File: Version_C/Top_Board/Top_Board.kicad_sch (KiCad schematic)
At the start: 12 parts, among them J1 90_Deg_Conn, J2 ADS1015, J4 90_Deg_Conn, U1 T-Display-S3

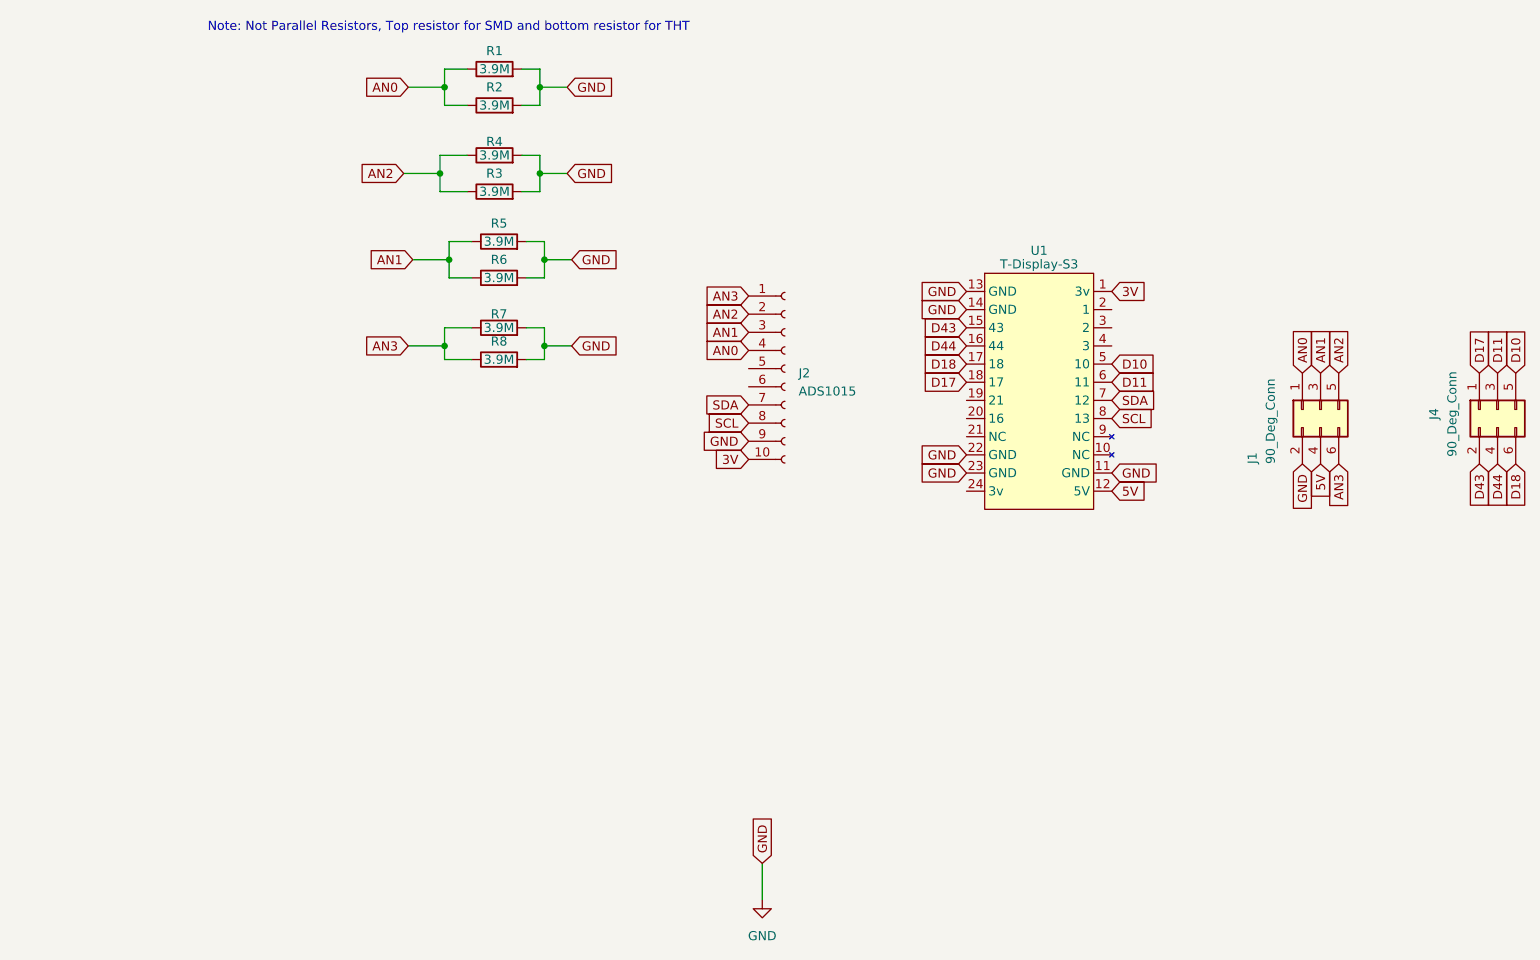
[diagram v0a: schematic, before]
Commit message: fixed directory overwrite
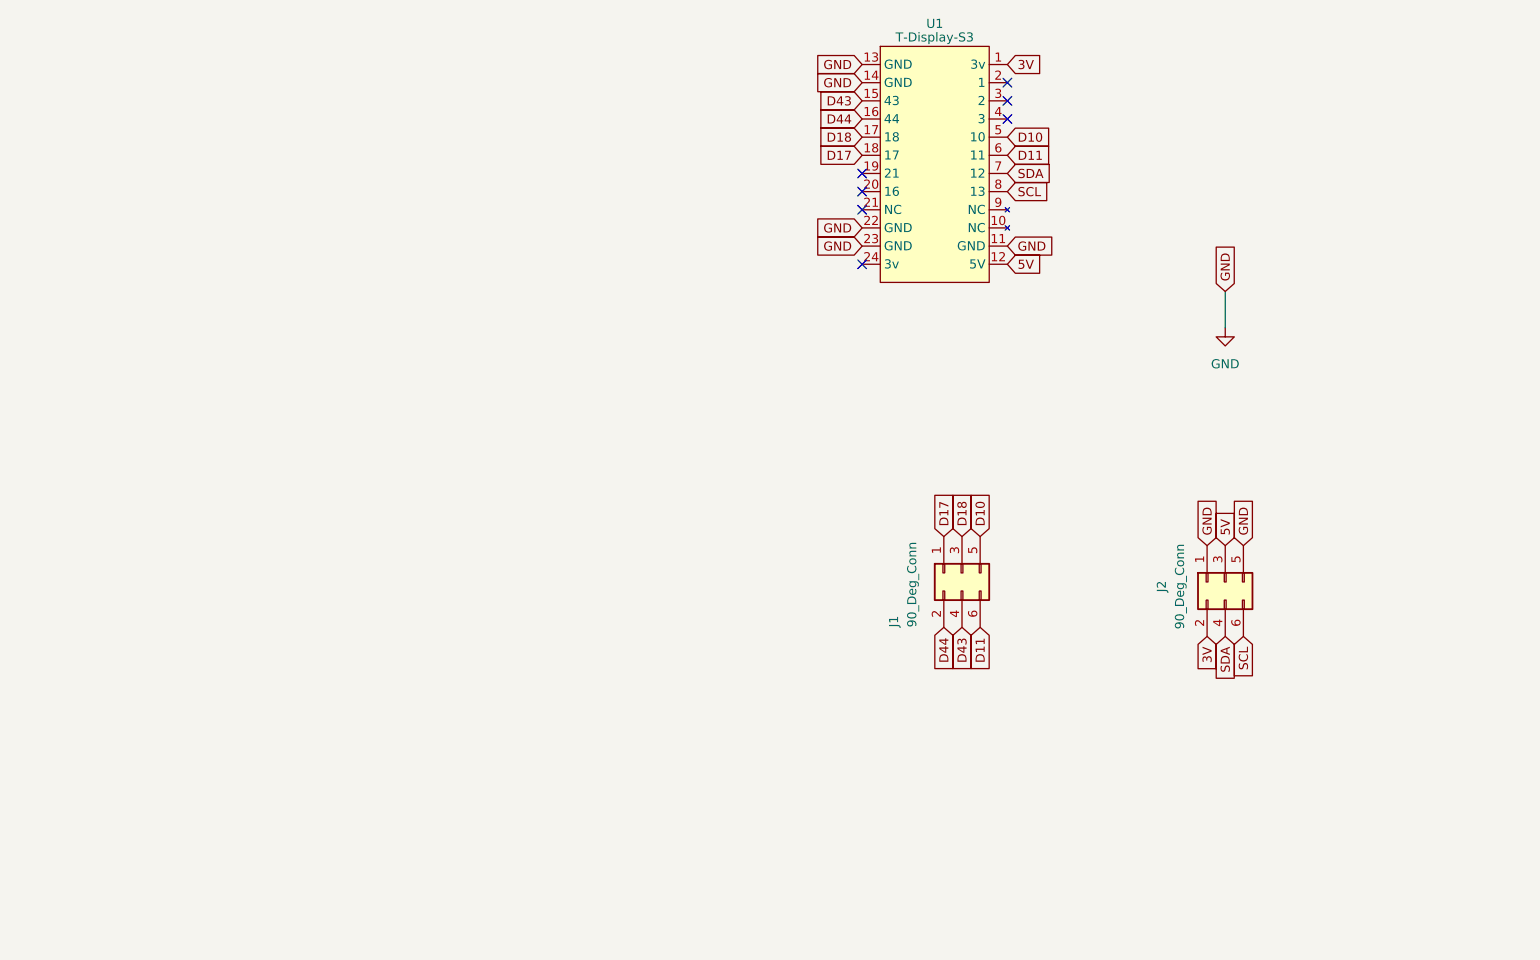
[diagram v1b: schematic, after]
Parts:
- removed J2: ADS1015, Voltage_Sensor_Timer:PinSocket_1x10_P2.54mm_Vertical_1, symbol Connector:Conn_01x10_Socket
- removed R1, R4, R5, R7: 3.9M, Resistor_SMD:R_0805_2012Metric, symbol Device:R
- removed R2, R3, R6, R8: 3.9M, Resistor_THT:R_Axial_DIN0411_L9.9mm_D3.6mm_P12.70mm_Horizontal, symbol Device:R
- renumbered J4 to J2
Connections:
- net AN0 is gone; now on net D17: J1.1 (Pin_1)
- net AN1 is gone; now on net D18: J1.3 (Pin_3)
- net AN2 is gone; now on net D10: J1.5 (Pin_5)
- net AN3 is gone; now on net D11: J1.6 (Pin_6)
- net 3V: now also J2.2 (Pin_2)
- net 5V: now also J2.3 (Pin_3); no longer J1.4 (Pin_4)
- net D10: no longer J2.5 (Pin_5)
- net D11: no longer J2.3 (Pin_3)
- net D17: no longer J2.1 (Pin_1)
- net D18: no longer J2.6 (Pin_6)
- net D43: now also J1.4 (Pin_4); no longer J2.2 (Pin_2)
- net D44: now also J1.2 (Pin_2); no longer J2.4 (Pin_4)
- net GND: now also J2.1 (Pin_1), J2.5 (Pin_5); no longer J1.2 (Pin_2)
- net SCL: now also J2.6 (Pin_6)
- net SDA: now also J2.4 (Pin_4)
- no-connect marks 0 -> 7
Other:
- note removed: "Note: Not Parallel Resistors, Top resistor for SMD and bottom resistor for THT"
- company: (none) -> Secured Solutions Group
- title: Top_Board -> Current Monitoring System (Top Board)
- moved on the sheet: J1, J2, U1
